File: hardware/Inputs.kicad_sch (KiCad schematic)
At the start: 0 parts

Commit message: Assign footprints to some components and improvements.
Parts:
- added C1: 100nF, Capacitor_SMD:C_0805_2012Metric_Pad1.18x1.45mm_HandSolder, symbol Device:C
- added C2, C3, C4, C5: C, Capacitor_SMD:C_0805_2012Metric_Pad1.18x1.45mm_HandSolder, symbol Device:C
- added D6, D7, D8, D9: SMF24A, Diode_SMD:D_SMF, symbol Diode:SMF24A
- added J1 (x2), J2, J3: Screw_Terminal_01x03, symbol Connector:Screw_Terminal_01x03
- added R10, R12, R13, R14, R15, R16, R17, R18: R, Resistor_SMD:R_0805_2012Metric_Pad1.20x1.40mm_HandSolder, symbol Device:R
- added R11, R7, R9: 150, Resistor_SMD:R_0805_2012Metric_Pad1.20x1.40mm_HandSolder, symbol Device:R
- added R8: 10K, Resistor_SMD:R_0805_2012Metric_Pad1.20x1.40mm_HandSolder, symbol Device:R
- added TP1, TP2, TP3, TP4: TestPoint, symbol Connector:TestPoint
- added U1, U2 (x4): MCP6004, Package_SO:SOIC-14_3.9x8.7mm_P1.27mm, symbol Amplifier_Operational:MCP6004
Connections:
- new net: D8.1 (A1), J2.2 (Pin_2), R11.1, R12.1
- new net: C5.1, R14.2, U2.3 (+)
- new net: D7.1 (A1), J1.2 (Pin_2), R10.1, R9.1
- new net: D6.1 (A1), J1.2 (Pin_2), R7.1, R8.1
- new net: C1.1, R8.2, U2.3 (+)
- new net: C3.1, R10.2, U2.3 (+)
- new net: D9.1 (A1), J3.2 (Pin_2), R13.1, R14.1
- new net: C4.1, R12.2, U2.3 (+)
- new net +24V: J1.1 (Pin_1), J1.1 (Pin_1), J2.1 (Pin_1), J3.1 (Pin_1)
- new net +3.3V: C2.1, U1.4 (V+)
- new net ANALOG1: R15.1, TP1.1, U2.1, U2.2 (-)
- new net ANALOG2: R16.1, TP2.1, U2.1, U2.2 (-)
- new net ANALOG3: R17.1, TP3.1, U2.1, U2.2 (-)
- new net ANALOG4: R18.1, TP4.1, U2.1, U2.2 (-)
- new net GND: C1.2, C2.2, C3.2, C4.2, C5.2, D6.2 (A2), D7.2 (A2), D8.2 (A2), D9.2 (A2), J1.3 (Pin_3), J1.3 (Pin_3), J2.3 (Pin_3), J3.3 (Pin_3), R11.2, R13.2, R15.2, R16.2, R17.2, R18.2, R7.2, R9.2, U1.11 (V-)

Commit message: Improvements to schematic.
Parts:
- added C? (x4): 100nF, Capacitor_SMD:C_0805_2012Metric_Pad1.18x1.45mm_HandSolder, symbol Device:C
- added D? (x4): ESD9B5.0ST5G, Diode_SMD:D_SOD-923, symbol Diode:ESD9B5.0ST5G
- added D? (x8): BZT52Bxx, Diode_SMD:D_SOD-123F, symbol Diode:BZT52Bxx
- added D? (x4): SS14, Diode_SMD:D_SMA, symbol Diode:SS14
- added J? (x4): Screw_Terminal_01x02, symbol Connector:Screw_Terminal_01x02
- added Q? (x4): 2N7002, Package_TO_SOT_SMD:SOT-23, symbol Transistor_FET:2N7002
- added R? (x4): 4.7K, symbol Device:R
- added R? (x4): 100K, symbol Device:R
- added R? (x8): 10K, symbol Device:R
- added R? (x4): R, symbol Device:R
- renumbered J1 to J?, TP4 to TP?, TP1 to TP?, TP2 to TP?, TP3 to TP?, U1 to U?
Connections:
- net +3.3V: now also R?.1, R?.1, R?.1, R?.1; no longer U?.4 (V+)
- net ANALOG2: now also U2.6 (-), U2.7; no longer U2.1, U2.2 (-)
- net ANALOG3: now also U2.8, U2.9 (-); no longer U2.1, U2.2 (-)
- net ANALOG4: now also U2.13 (-), U2.14; no longer U2.1, U2.2 (-)
- net GND: now also C?.2, C?.2, C?.2, C?.2, D?.1 (A1), D?.1 (A1), D?.1 (A1), D?.1 (A1), D?.1 (K), D?.1 (K), D?.1 (K), D?.1 (K), J?.2 (Pin_2), J?.2 (Pin_2), J?.2 (Pin_2), J?.2 (Pin_2), Q?.2 (S), Q?.2 (S), Q?.2 (S), Q?.2 (S), R?.2, R?.2, R?.2, R?.2; no longer U?.11 (V-)
- net at C5.1, R14.2: now also U2.12 (+); no longer U2.3 (+)
- net at C3.1, R10.2: now also U2.5 (+); no longer U2.3 (+)
- net at C4.1, R12.2: now also U2.10 (+); no longer U2.3 (+)
- new net: D?.1 (K), R?.1, R?.2 (x4)
- new net: D?.1 (K), Q?.1 (G), R?.1, R?.2 (x4)
- new net: D?.2 (A), D?.2 (A2), J?.1 (Pin_1), R?.1 (x4)
- new net: Q?.3 (D), R?.1, R?.2 (x4)
- new net: D?.2 (A), D?.2 (A) (x4)
- new net Digital_In_1: C?.1, R?.2
- new net Digital_In_2: C?.1, R?.2
- new net Digital_In_3: C?.1, R?.2
- new net Digital_In_4: C?.1, R?.2
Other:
- note added: "Analog Inputs"
- note added: "Digital Inputs"
- company: (none) -> FEYTECH PTY LTD
- title: (none) -> MQTT Gateway
- moved on the sheet: C1, C2, C3, C4, C5, D6, D7, D8, D9, J1, J2, J3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

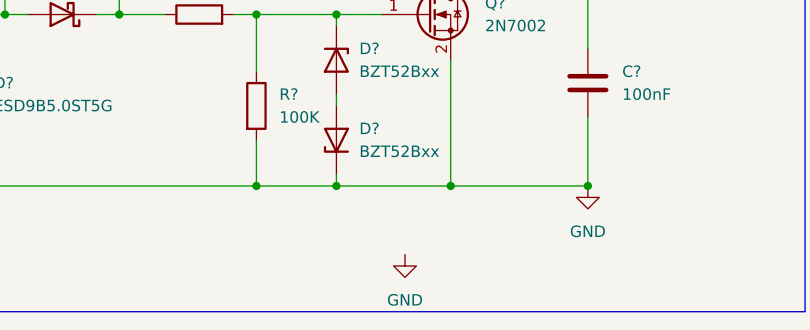
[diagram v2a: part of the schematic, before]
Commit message: Add footprint to components
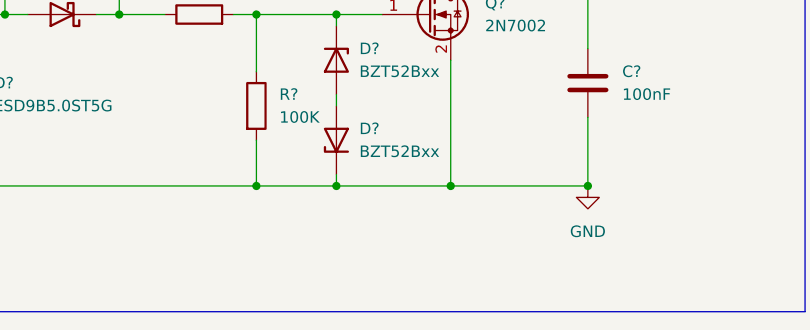
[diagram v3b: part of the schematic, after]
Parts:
- C1, C2, C3, C4, C5, C? (x4): footprint Capacitor_SMD:C_0805_2012Metric_Pad1.18x1.45mm_HandSolder -> Capacitor_SMD:C_0603_1608Metric_Pad1.08x0.95mm_HandSolder
- R10, R11, R12, R13, R14, R15, R16, R17, R18, R7, R8, R9: footprint Resistor_SMD:R_0805_2012Metric_Pad1.20x1.40mm_HandSolder -> Resistor_SMD:R_0603_1608Metric_Pad0.98x0.95mm_HandSolder
- R? (x15): footprint (none) -> Resistor_SMD:R_0603_1608Metric_Pad0.98x0.95mm_HandSolder
- TP? (x4): footprint (none) -> TestPoint:TestPoint_Pad_D1.0mm
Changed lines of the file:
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@@
 			)
 		)
-		(property "Footprint" ""
+		(property "Footprint" "Resistor_SMD:R_0603_1608Metric_Pad0.98x0.95mm_HandSolder"
 			(at 63.5 79.248 90)
 			(effects
@@
 			)
 		)
-		(property "Footprint" ""
+		(property "Footprint" "Resistor_SMD:R_0603_1608Metric_Pad0.98x0.95mm_HandSolder"
 			(at 68.072 173.99 90)
 			(effects
@@
 			)
 		)
-		(property "Footprint" ""
+		(property "Footprint" "TestPoint:TestPoint_Pad_D1.0mm"
 			(at 264.16 129.54 0)
 			(effects
@@
 			)
 		)
-		(property "Footprint" ""
+		(property "Footprint" "TestPoint:TestPoint_Pad_D1.0mm"
 			(at 262.89 34.29 0)
 			(effects
@@
 			)
 		)
-		(property "Footprint" "Capacitor_SMD:C_0805_2012Metric_Pad1.18x1.45mm_HandSolder"
+		(property "Footprint" "Capacitor_SMD:C_0603_1608Metric_Pad1.08x0.95mm_HandSolder"
 			(at 224.4852 140.97 0)
 			(effects
@@
 			)
 		)
-		(property "Footprint" "Resistor_SMD:R_0805_2012Metric_Pad1.20x1.40mm_HandSolder"
+		(property "Footprint" "Resistor_SMD:R_0603_1608Metric_Pad0.98x0.95mm_HandSolder"
 			(at 252.222 138.43 90)
 			(effects
@@
 			)
 		)
-		(property "Footprint" "Resistor_SMD:R_0805_2012Metric_Pad1.20x1.40mm_HandSolder"
+		(property "Footprint" "Resistor_SMD:R_0603_1608Metric_Pad0.98x0.95mm_HandSolder"
 			(at 250.952 106.68 90)
 			(effects
@@
 			)
 		)
-		(property "Footprint" ""
+		(property "Footprint" "Resistor_SMD:R_0603_1608Metric_Pad0.98x0.95mm_HandSolder"
 			(at 100.33 72.898 90)
 			(effects
@@
 			)
 		)
-		(property "Footprint" "Resistor_SMD:R_0805_2012Metric_Pad1.20x1.40mm_HandSolder"
+		(property "Footprint" "Resistor_SMD:R_0603_1608Metric_Pad0.98x0.95mm_HandSolder"
 			(at 196.342 138.43 90)
 			(effects
@@
 			)
 		)
-		(property "Footprint" "Capacitor_SMD:C_0805_2012Metric_Pad1.18x1.45mm_HandSolder"
+		(property "Footprint" "Capacitor_SMD:C_0603_1608Metric_Pad1.08x0.95mm_HandSolder"
 			(at 224.4852 109.22 0)
 			(effects
@@
 			)
 		)
-		(property "Footprint" ""
+		(property "Footprint" "Resistor_SMD:R_0603_1608Metric_Pad0.98x0.95mm_HandSolder"
 			(at 63.5 165.608 90)
 			(effects
@@
 			)
 		)
-		(property "Footprint" ""
+		(property "Footprint" "Resistor_SMD:R_0603_1608Metric_Pad0.98x0.95mm_HandSolder"
 			(at 100.33 30.988 90)
 			(effects
@@
 			)
 		)
-		(property "Footprint" "Resistor_SMD:R_0805_2012Metric_Pad1.20x1.40mm_HandSolder"
+		(property "Footprint" "Resistor_SMD:R_0603_1608Metric_Pad0.98x0.95mm_HandSolder"
 			(at 196.342 43.18 90)
 			(effects
@@
 			)
 		)
-		(property "Footprint" "Capacitor_SMD:C_0805_2012Metric_Pad1.18x1.45mm_HandSolder"
+		(property "Footprint" "Capacitor_SMD:C_0603_1608Metric_Pad1.08x0.95mm_HandSolder"
 			(at 107.6452 46.99 0)
 			(effects
@@
 			)
 		)
-		(property "Footprint" ""
+		(property "Footprint" "Resistor_SMD:R_0603_1608Metric_Pad0.98x0.95mm_HandSolder"
 			(at 89.662 152.4 90)
 			(effects
@@
 			)
 		)
-		(property "Footprint" ""
+		(property "Footprint" "Resistor_SMD:R_0603_1608Metric_Pad0.98x0.95mm_HandSolder"
 			(at 89.662 66.04 90)
 			(effects
@@
 			)
 		)
-		(property "Footprint" "Resistor_SMD:R_0805_2012Metric_Pad1.20x1.40mm_HandSolder"
+		(property "Footprint" "Resistor_SMD:R_0603_1608Metric_Pad0.98x0.95mm_HandSolder"
 			(at 196.342 106.68 90)
 			(effects
@@
 			)
 		)
-		(property "Footprint" ""
+		(property "Footprint" "TestPoint:TestPoint_Pad_D1.0mm"
 			(at 262.89 66.04 0)
 			(effects
@@
 			)
 		)
-		(property "Footprint" "Resistor_SMD:R_0805_2012Metric_Pad1.20x1.40mm_HandSolder"
+		(property "Footprint" "Resistor_SMD:R_0603_1608Metric_Pad0.98x0.95mm_HandSolder"
 			(at 214.63 70.358 90)
 			(effects
@@
 			)
 		)
-		(property "Footprint" "Capacitor_SMD:C_0805_2012Metric_Pad1.18x1.45mm_HandSolder"
+		(property "Footprint" "Capacitor_SMD:C_0603_1608Metric_Pad1.08x0.95mm_HandSolder"
 			(at 107.6452 88.9 0)
 			(effects
@@
 			)
 		)
-		(property "Footprint" "Capacitor_SMD:C_0805_2012Metric_Pad1.18x1.45mm_HandSolder"
+		(property "Footprint" "Capacitor_SMD:C_0603_1608Metric_Pad1.08x0.95mm_HandSolder"
 			(at 168.6052 87.63 0)
 			(effects
@@
 			)
 		)
-		(property "Footprint" "Capacitor_SMD:C_0805_2012Metric_Pad1.18x1.45mm_HandSolder"
+		(property "Footprint" "Capacitor_SMD:C_0603_1608Metric_Pad1.08x0.95mm_HandSolder"
 			(at 107.6452 175.26 0)
 			(effects
@@
 			)
 		)
-		(property "Footprint" "Capacitor_SMD:C_0805_2012Metric_Pad1.18x1.45mm_HandSolder"
+		(property "Footprint" "Capacitor_SMD:C_0603_1608Metric_Pad1.08x0.95mm_HandSolder"
 			(at 224.4852 77.47 0)
 			(effects
@@
 			)
 		)
-		(property "Footprint" ""
+		(property "Footprint" "Resistor_SMD:R_0603_1608Metric_Pad0.98x0.95mm_HandSolder"
 			(at 48.26 69.088 90)
 			(effects
@@
 			)
 		)
-		(property "Footprint" "Resistor_SMD:R_0805_2012Metric_Pad1.20x1.40mm_HandSolder"
+		(property "Footprint" "Resistor_SMD:R_0603_1608Metric_Pad0.98x0.95mm_HandSolder"
 			(at 250.952 43.18 90)
 			(effects
@@
 			)
 		)
-		(property "Footprint" ""
+		(property "Footprint" "Resistor_SMD:R_0603_1608Metric_Pad0.98x0.95mm_HandSolder"
 			(at 68.072 87.63 90)
 			(effects
@@
 			)
 		)
-		(property "Footprint" ""
+		(property "Footprint" "Resistor_SMD:R_0603_1608Metric_Pad0.98x0.95mm_HandSolder"
 			(at 68.072 45.72 90)
 			(effects
@@
 			)
 		)
-		(property "Footprint" "Resistor_SMD:R_0805_2012Metric_Pad1.20x1.40mm_HandSolder"
+		(property "Footprint" "Resistor_SMD:R_0603_1608Metric_Pad0.98x0.95mm_HandSolder"
 			(at 214.63 38.608 90)
 			(effects
@@
 			)
 		)
-		(property "Footprint" ""
+		(property "Footprint" "Resistor_SMD:R_0603_1608Metric_Pad0.98x0.95mm_HandSolder"
 			(at 89.662 24.13 90)
 			(effects
@@
 			)
 		)
-		(property "Footprint" ""
+		(property "Footprint" "TestPoint:TestPoint_Pad_D1.0mm"
 			(at 264.16 97.79 0)
 			(effects
@@
 			)
 		)
-		(property "Footprint" "Resistor_SMD:R_0805_2012Metric_Pad1.20x1.40mm_HandSolder"
+		(property "Footprint" "Resistor_SMD:R_0603_1608Metric_Pad0.98x0.95mm_HandSolder"
 			(at 214.63 133.858 90)
 			(effects
@@
 			)
 		)
-		(property "Footprint" ""
+		(property "Footprint" "Resistor_SMD:R_0603_1608Metric_Pad0.98x0.95mm_HandSolder"
 			(at 48.26 155.448 90)
 			(effects
@@
 	)
 	(symbol
-		(lib_id "power:GND")
-		(at 86.36 190.5 0)
-		(unit 1)
-		(exclude_from_sim no)
-		(in_bom yes)
-		(on_board yes)
-		(dnp no)
-		(fields_autoplaced yes)
-		(property "Reference" "#PWR?"
-			(at 86.36 196.85 0)
-			(effects
-				(font
-					(size 1.27 1.27)
-				)
-				(hide yes)
-			)
-		)
-		(property "Value" "GND"
-			(at 86.36 195.58 0)
-			(effects
-				(font
-					(size 1.27 1.27)
-				)
-			)
-		)
-		(property "Footprint" ""
-			(at 86.36 190.5 0)
-			(effects
-				(font
-					(size 1.27 1.27)
-				)
-				(hide yes)
-			)
-		)
-		(property "Datasheet" ""
-			(at 86.36 190.5 0)
-			(effects
-				(font
-					(size 1.27 1.27)
-				)
-				(hide yes)
-			)
-		)
-		(property "Description" "Power symbol creates a global label with name \"GND\" , ground"
-			(at 86.36 190.5 0)
-			(effects
-				(font
-					(size 1.27 1.27)
-				)
-				(hide yes)
-			)
-		)
-		(pin "1"
-		)
-		(instances
-			(project "MQTTGateway"
-				(path "/05707d4e-3d4a-41f6-9822-862f6f3b507e/05fd85a5-633a-4085-b17c-4093445eb99c"
-					(reference "#PWR?")
-					(unit 1)
-				)
-			)
-			(project "Inputs"
-				(path "/10b29416-f9ea-4062-9ef8-c88a86feafdf"
-					(reference "#PWR?")
-					(unit 1)
-				)
-			)
-		)
-	)
-	(symbol
 		(lib_id "Device:R")
 		(at 214.63 100.33 90)
@@
 			)
 		)
-		(property "Footprint" "Resistor_SMD:R_0805_2012Metric_Pad1.20x1.40mm_HandSolder"
+		(property "Footprint" "Resistor_SMD:R_0603_1608Metric_Pad0.98x0.95mm_HandSolder"
 			(at 214.63 102.108 90)
 			(effects
@@
 			)
 		)
-		(property "Footprint" ""
+		(property "Footprint" "Resistor_SMD:R_0603_1608Metric_Pad0.98x0.95mm_HandSolder"
 			(at 63.5 37.338 90)
 			(effects
@@
 			)
 		)
-		(property "Footprint" "Resistor_SMD:R_0805_2012Metric_Pad1.20x1.40mm_HandSolder"
+		(property "Footprint" "Resistor_SMD:R_0603_1608Metric_Pad0.98x0.95mm_HandSolder"
 			(at 250.952 74.93 90)
 			(effects
@@
 			)
 		)
-		(property "Footprint" "Capacitor_SMD:C_0805_2012Metric_Pad1.18x1.45mm_HandSolder"
+		(property "Footprint" "Capacitor_SMD:C_0603_1608Metric_Pad1.08x0.95mm_HandSolder"
 			(at 224.4852 45.72 0)
 			(effects
@@
 			)
 		)
-		(property "Footprint" "Capacitor_SMD:C_0805_2012Metric_Pad1.18x1.45mm_HandSolder"
+		(property "Footprint" "Capacitor_SMD:C_0603_1608Metric_Pad1.08x0.95mm_HandSolder"
 			(at 107.6452 130.81 0)
 			(effects
@@
 			)
 		)
-		(property "Footprint" "Resistor_SMD:R_0805_2012Metric_Pad1.20x1.40mm_HandSolder"
+		(property "Footprint" "Resistor_SMD:R_0603_1608Metric_Pad0.98x0.95mm_HandSolder"
 			(at 196.342 74.93 90)
 			(effects
@@
 			)
 		)
-		(property "Footprint" ""
+		(property "Footprint" "Resistor_SMD:R_0603_1608Metric_Pad0.98x0.95mm_HandSolder"
 			(at 100.33 159.258 90)
 			(effects
@@
 			)
 		)
-		(property "Footprint" ""
+		(property "Footprint" "Resistor_SMD:R_0603_1608Metric_Pad0.98x0.95mm_HandSolder"
 			(at 48.26 27.178 90)
 			(effects

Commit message: Improvements
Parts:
- removed U2, U?: MCP6004, Package_SO:SOIC-14_3.9x8.7mm_P1.27mm, symbol Amplifier_Operational:MCP6004
- added U10, U11, U12, U13, U14: MCP6004, symbol Amplifier_Operational:MCP6004
- J10: renamed from J?; footprint (none) -> TerminalBlock_Phoenix:TerminalBlock_Phoenix_MKDS-1,5-3-5.08_1x03_P5.08mm_Horizontal
- J11: renamed from J1; footprint (none) -> TerminalBlock_Phoenix:TerminalBlock_Phoenix_MKDS-1,5-3-5.08_1x03_P5.08mm_Horizontal
- J12: renamed from J2; footprint (none) -> TerminalBlock_Phoenix:TerminalBlock_Phoenix_MKDS-1,5-3-5.08_1x03_P5.08mm_Horizontal
- J13: renamed from J3; footprint (none) -> TerminalBlock_Phoenix:TerminalBlock_Phoenix_MKDS-1,5-3-5.08_1x03_P5.08mm_Horizontal
- J6, J7, J8, J9: renamed from J?; footprint (none) -> TerminalBlock_Phoenix:TerminalBlock_Phoenix_MKDS-1,5-2-5.08_1x02_P5.08mm_Horizontal
- R37, R38, R40: renamed from R?; value R -> 0
- R39: renamed from R?; value R -> 0; footprint (none) -> Resistor_SMD:R_0603_1608Metric_Pad0.98x0.95mm_HandSolder
- R43, R47, R51, R55: renamed from R?; footprint (none) -> Resistor_SMD:R_0603_1608Metric_Pad0.98x0.95mm_HandSolder
- R60: renamed from R13; value R -> 150
- R62: renamed from R10; value R -> 10K
- R63: renamed from R12; value R -> 10K
- R64: renamed from R14; value R -> 10K
- R65: renamed from R15; value R -> 47K
- R66: renamed from R16; value R -> 47K
- R67: renamed from R17; value R -> 47K
- R68: renamed from R18; value R -> 47K
- gave numbers to parts that had none: 40
- renumbered C2 to C63, C1 to C64, C3 to C65, C4 to C66, C5 to C67, D6 to D30, D7 to D31, D8 to D32, D9 to D33, R7 to R57, R9 to R58, R11 to R59, R8 to R61
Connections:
- net ANALOG1: now also U11.1, U11.2 (-)
- net ANALOG2: now also U12.1, U12.2 (-)
- net ANALOG3: now also U13.1, U13.2 (-)
- net ANALOG4: now also U14.1, U14.2 (-)
- net at C67.1, R64.2: now also U14.3 (+)
- net at C64.1, R61.2: now also U11.3 (+)
- net at C65.1, R62.2: now also U12.3 (+)
- net at C66.1, R63.2: now also U13.3 (+)

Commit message: More improvements
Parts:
- U10: footprint (none) -> Package_SO:SOIC-14_3.9x8.7mm_P1.27mm
- U10: renamed from U14; footprint (none) -> Package_SO:SOIC-14_3.9x8.7mm_P1.27mm
- U10: renamed from U11; footprint (none) -> Package_SO:SOIC-14_3.9x8.7mm_P1.27mm
- U10: renamed from U12; footprint (none) -> Package_SO:SOIC-14_3.9x8.7mm_P1.27mm
- U10: renamed from U13; footprint (none) -> Package_SO:SOIC-14_3.9x8.7mm_P1.27mm
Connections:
- net +3.3V: now also U10.4 (V+)
- net ANALOG2: now also U10.6 (-), U10.7; no longer U10.1, U10.2 (-)
- net ANALOG3: now also U10.8, U10.9 (-); no longer U10.1, U10.2 (-)
- net ANALOG4: now also U10.13 (-), U10.14; no longer U10.1, U10.2 (-)
- net GND: now also U10.11 (V-)
- net at C67.1, R64.2: now also U10.12 (+); no longer U10.3 (+)
- net at C66.1, R63.2: now also U10.10 (+); no longer U10.3 (+)
- net at C65.1, R62.2: now also U10.5 (+); no longer U10.3 (+)
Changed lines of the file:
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@@
 		(lib_id "Amplifier_Operational:MCP6004")
 		(at 156.21 83.82 0)
-		(unit 1)
+		(unit 5)
 		(exclude_from_sim no)
 		(in_bom yes)
@@
 			)
 		)
-		(property "Footprint" ""
+		(property "Footprint" "Package_SO:SOIC-14_3.9x8.7mm_P1.27mm"
 			(at 154.94 81.28 0)
 			(effects
@@
 				(path "/05707d4e-3d4a-41f6-9822-862f6f3b507e/05fd85a5-633a-4085-b17c-4093445eb99c"
 					(reference "U10")
-					(unit 1)
+					(unit 5)
 				)
 			)
@@
 		(at 240.03 129.54 0)
 		(mirror x)
-		(unit 1)
+		(unit 4)
 		(exclude_from_sim no)
 		(in_bom yes)
 		(on_board yes)
 		(dnp no)
-		(property "Reference" "U14"
+		(property "Reference" "U10"
 			(at 240.03 139.7 0)
 			(effects
@@
 			)
 		)
-		(property "Footprint" ""
+		(property "Footprint" "Package_SO:SOIC-14_3.9x8.7mm_P1.27mm"
 			(at 238.76 132.08 0)
 			(effects
@@
 			(project "MQTTGateway"
 				(path "/05707d4e-3d4a-41f6-9822-862f6f3b507e/05fd85a5-633a-4085-b17c-4093445eb99c"
-					(reference "U14")
-					(unit 1)
+					(reference "U10")
+					(unit 4)
 				)
 			)
@@
 		(on_board yes)
 		(dnp no)
-		(property "Reference" "U11"
+		(property "Reference" "U10"
 			(at 240.03 44.45 0)
 			(effects
@@
 			)
 		)
-		(property "Footprint" ""
+		(property "Footprint" "Package_SO:SOIC-14_3.9x8.7mm_P1.27mm"
 			(at 238.76 36.83 0)
 			(effects
@@
 			(project "MQTTGateway"
 				(path "/05707d4e-3d4a-41f6-9822-862f6f3b507e/05fd85a5-633a-4085-b17c-4093445eb99c"
-					(reference "U11")
+					(reference "U10")
 					(unit 1)
 				)
@@
 		(at 240.03 66.04 0)
 		(mirror x)
-		(unit 1)
+		(unit 2)
 		(exclude_from_sim no)
 		(in_bom yes)
 		(on_board yes)
 		(dnp no)
-		(property "Reference" "U12"
+		(property "Reference" "U10"
 			(at 240.03 76.2 0)
 			(effects
@@
 			)
 		)
-		(property "Footprint" ""
+		(property "Footprint" "Package_SO:SOIC-14_3.9x8.7mm_P1.27mm"
 			(at 238.76 68.58 0)
 			(effects
@@
 			(project "MQTTGateway"
 				(path "/05707d4e-3d4a-41f6-9822-862f6f3b507e/05fd85a5-633a-4085-b17c-4093445eb99c"
-					(reference "U12")
-					(unit 1)
+					(reference "U10")
+					(unit 2)
 				)
 			)
@@
 		(at 240.03 97.79 0)
 		(mirror x)
-		(unit 1)
+		(unit 3)
 		(exclude_from_sim no)
 		(in_bom yes)
 		(on_board yes)
 		(dnp no)
-		(property "Reference" "U13"
+		(property "Reference" "U10"
 			(at 240.03 107.95 0)
 			(effects
@@
 			)
 		)
-		(property "Footprint" ""
+		(property "Footprint" "Package_SO:SOIC-14_3.9x8.7mm_P1.27mm"
 			(at 238.76 100.33 0)
 			(effects
@@
 			(project "MQTTGateway"
 				(path "/05707d4e-3d4a-41f6-9822-862f6f3b507e/05fd85a5-633a-4085-b17c-4093445eb99c"
-					(reference "U13")
-					(unit 1)
+					(reference "U10")
+					(unit 3)
 				)
 			)
